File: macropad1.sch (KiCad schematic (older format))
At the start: 20 parts, among them J1 Conn_01x04, J2 USB_B_Mini, J3 AVR-ISP-6, SW1 SPST, SW2 Rotary_Encoder_Switch, U1 ATmega32U4-AU, U2 24LC512, Y1 16Mhz

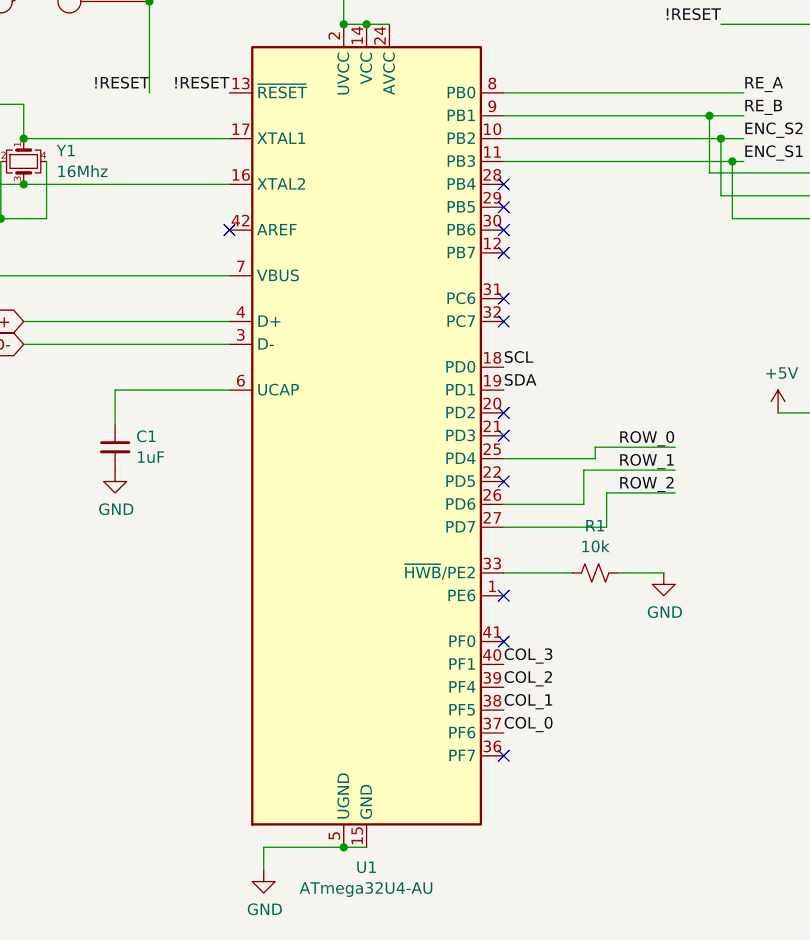
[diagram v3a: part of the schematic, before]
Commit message: Adds testpads for all unused pins on MCU
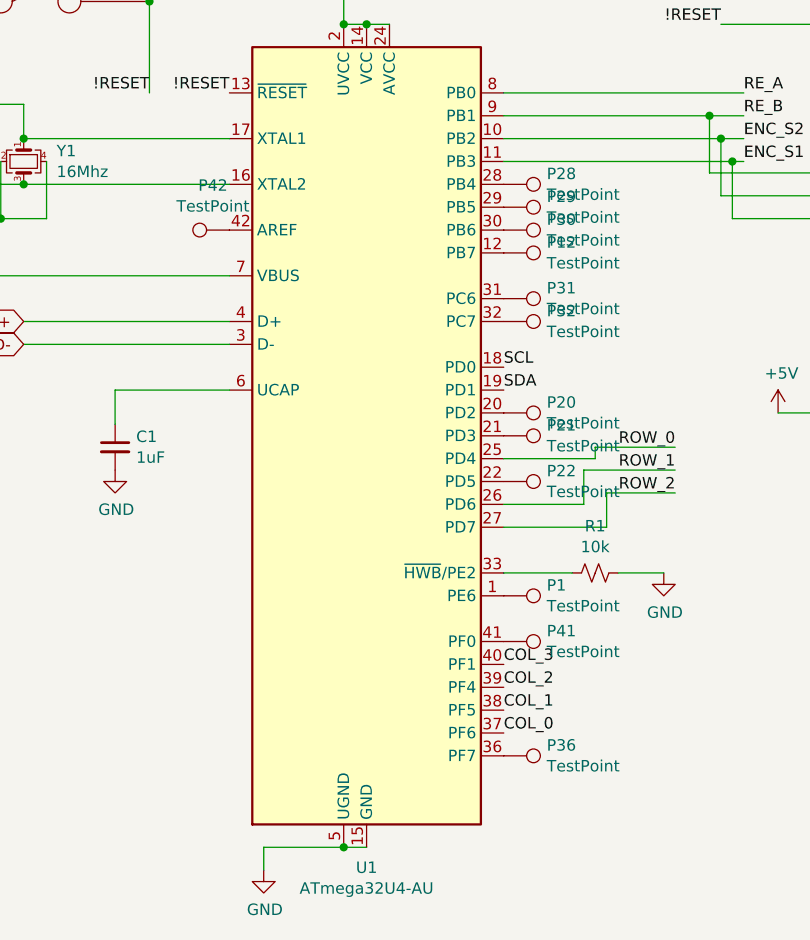
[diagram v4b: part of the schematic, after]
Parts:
- added P1, P12, P20, P21, P22, P28, P29, P30, P31, P32, P36, P41, P42: TestPoint, TestPoint:TestPoint_Pad_D1.0mm, symbol Connector:TestPoint
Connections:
- net at U1.1 (PE6): now also P1.1
- net at U1.12 (PB7): now also P12.1
- net at U1.20 (PD2): now also P20.1
- net at U1.21 (PD3): now also P21.1
- net at U1.22 (PD5): now also P22.1
- net at U1.28 (PB4): now also P28.1
- net at U1.29 (PB5): now also P29.1
- net at U1.30 (PB6): now also P30.1
- net at U1.31 (PC6): now also P31.1
- net at U1.32 (PC7): now also P32.1
- net at U1.36 (PF7): now also P36.1
- net at U1.41 (PF0): now also P41.1
- net at U1.42 (AREF): now also P42.1
- no-connect marks 14 -> 1
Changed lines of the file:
@@
 	1    0    0    -1
 $EndComp
-NoConn ~ 4500 2600
-NoConn ~ 4500 2700
-NoConn ~ 4500 2800
-NoConn ~ 4500 2900
-NoConn ~ 4500 3100
-NoConn ~ 4500 3200
-NoConn ~ 4500 3600
-NoConn ~ 4500 3700
-NoConn ~ 4500 3900
-NoConn ~ 4500 4400
-NoConn ~ 4500 4600
-NoConn ~ 4500 5100
 Wire Wire Line
 	6200 1450 6300 1450
@@
 Connection ~ 7250 4050
 NoConn ~ 7650 3850
-NoConn ~ 3300 2800
 Wire Wire Line
 	3300 3000 1150 3000
@@
 Wire Wire Line
 	6950 2150 6500 2150
+$Comp
+L Connector:TestPoint P28
+U 1 1 5F6F4AA3
+P 4500 2600
+F 0 "P28" V 4454 2788 50  0000 L CNN
+F 1 "TestPoint" V 4545 2788 50  0000 L CNN
+F 2 "TestPoint:TestPoint_Pad_D1.0mm" H 4700 2600 50  0001 C CNN
+F 3 "~" H 4700 2600 50  0001 C CNN
+	1    4500 2600
+	0    1    1    0
+$EndComp
+$Comp
+L Connector:TestPoint P29
+U 1 1 5F6F7A9F
+P 4500 2700
+F 0 "P29" V 4454 2888 50  0000 L CNN
+F 1 "TestPoint" V 4545 2888 50  0000 L CNN
+F 2 "TestPoint:TestPoint_Pad_D1.0mm" H 4700 2700 50  0001 C CNN
+F 3 "~" H 4700 2700 50  0001 C CNN
+	1    4500 2700
+	0    1    1    0
+$EndComp
+$Comp
+L Connector:TestPoint P30
+U 1 1 5F6F7EF0
+P 4500 2800
+F 0 "P30" V 4454 2988 50  0000 L CNN
+F 1 "TestPoint" V 4545 2988 50  0000 L CNN
+F 2 "TestPoint:TestPoint_Pad_D1.0mm" H 4700 2800 50  0001 C CNN
+F 3 "~" H 4700 2800 50  0001 C CNN
+	1    4500 2800
+	0    1    1    0
+$EndComp
+$Comp
+L Connector:TestPoint P12
+U 1 1 5F6F82A4
+P 4500 2900
+F 0 "P12" V 4454 3088 50  0000 L CNN
+F 1 "TestPoint" V 4545 3088 50  0000 L CNN
+F 2 "TestPoint:TestPoint_Pad_D1.0mm" H 4700 2900 50  0001 C CNN
+F 3 "~" H 4700 2900 50  0001 C CNN
+	1    4500 2900
+	0    1    1    0
+$EndComp
+$Comp
+L Connector:TestPoint P31
+U 1 1 5F6F8637
+P 4500 3100
+F 0 "P31" V 4454 3288 50  0000 L CNN
+F 1 "TestPoint" V 4545 3288 50  0000 L CNN
+F 2 "TestPoint:TestPoint_Pad_D1.0mm" H 4700 3100 50  0001 C CNN
+F 3 "~" H 4700 3100 50  0001 C CNN
+	1    4500 3100
+	0    1    1    0
+$EndComp
+$Comp
+L Connector:TestPoint P32
+U 1 1 5F6F8A2A
+P 4500 3200
+F 0 "P32" V 4454 3388 50  0000 L CNN
+F 1 "TestPoint" V 4545 3388 50  0000 L CNN
+F 2 "TestPoint:TestPoint_Pad_D1.0mm" H 4700 3200 50  0001 C CNN
+F 3 "~" H 4700 3200 50  0001 C CNN
+	1    4500 3200
+	0    1    1    0
+$EndComp
+$Comp
+L Connector:TestPoint P20
+U 1 1 5F6F8E3F
+P 4500 3600
+F 0 "P20" V 4454 3788 50  0000 L CNN
+F 1 "TestPoint" V 4545 3788 50  0000 L CNN
+F 2 "TestPoint:TestPoint_Pad_D1.0mm" H 4700 3600 50  0001 C CNN
+F 3 "~" H 4700 3600 50  0001 C CNN
+	1    4500 3600
+	0    1    1    0
+$EndComp
+$Comp
+L Connector:TestPoint P21
+U 1 1 5F6F92F7
+P 4500 3700
+F 0 "P21" V 4454 3888 50  0000 L CNN
+F 1 "TestPoint" V 4545 3888 50  0000 L CNN
+F 2 "TestPoint:TestPoint_Pad_D1.0mm" H 4700 3700 50  0001 C CNN
+F 3 "~" H 4700 3700 50  0001 C CNN
+	1    4500 3700
+	0    1    1    0
+$EndComp
+$Comp
+L Connector:TestPoint P22
+U 1 1 5F6F96DD
+P 4500 3900
+F 0 "P22" V 4454 4088 50  0000 L CNN
+F 1 "TestPoint" V 4545 4088 50  0000 L CNN
+F 2 "TestPoint:TestPoint_Pad_D1.0mm" H 4700 3900 50  0001 C CNN
+F 3 "~" H 4700 3900 50  0001 C CNN
+	1    4500 3900
+	0    1    1    0
+$EndComp
+$Comp
+L Connector:TestPoint P1
+U 1 1 5F6F9AE5
+P 4500 4400
+F 0 "P1" V 4454 4588 50  0000 L CNN
+F 1 "TestPoint" V 4545 4588 50  0000 L CNN
+F 2 "TestPoint:TestPoint_Pad_D1.0mm" H 4700 4400 50  0001 C CNN
+F 3 "~" H 4700 4400 50  0001 C CNN
+	1    4500 4400
+	0    1    1    0
+$EndComp
+$Comp
+L Connector:TestPoint P41
+U 1 1 5F6FA019
+P 4500 4600
+F 0 "P41" V 4454 4788 50  0000 L CNN
+F 1 "TestPoint" V 4545 4788 50  0000 L CNN
+F 2 "TestPoint:TestPoint_Pad_D1.0mm" H 4700 4600 50  0001 C CNN
+F 3 "~" H 4700 4600 50  0001 C CNN
+	1    4500 4600
+	0    1    1    0
+$EndComp
+$Comp
+L Connector:TestPoint P36
+U 1 1 5F6FC57F
+P 4500 5100
+F 0 "P36" V 4454 5288 50  0000 L CNN
+F 1 "TestPoint" V 4545 5288 50  0000 L CNN
+F 2 "TestPoint:TestPoint_Pad_D1.0mm" H 4700 5100 50  0001 C CNN
+F 3 "~" H 4700 5100 50  0001 C CNN
+	1    4500 5100
+	0    1    1    0
+$EndComp
+$Comp
+L Connector:TestPoint P42
+U 1 1 5F6FCA35
+P 3300 2800
+F 0 "P42" V 3495 2872 50  0000 C CNN
+F 1 "TestPoint" V 3404 2872 50  0000 C CNN
+F 2 "TestPoint:TestPoint_Pad_D1.0mm" H 3500 2800 50  0001 C CNN
+F 3 "~" H 3500 2800 50  0001 C CNN
+	1    3300 2800
+	0    -1   -1   0
+$EndComp
 $EndSCHEMATC

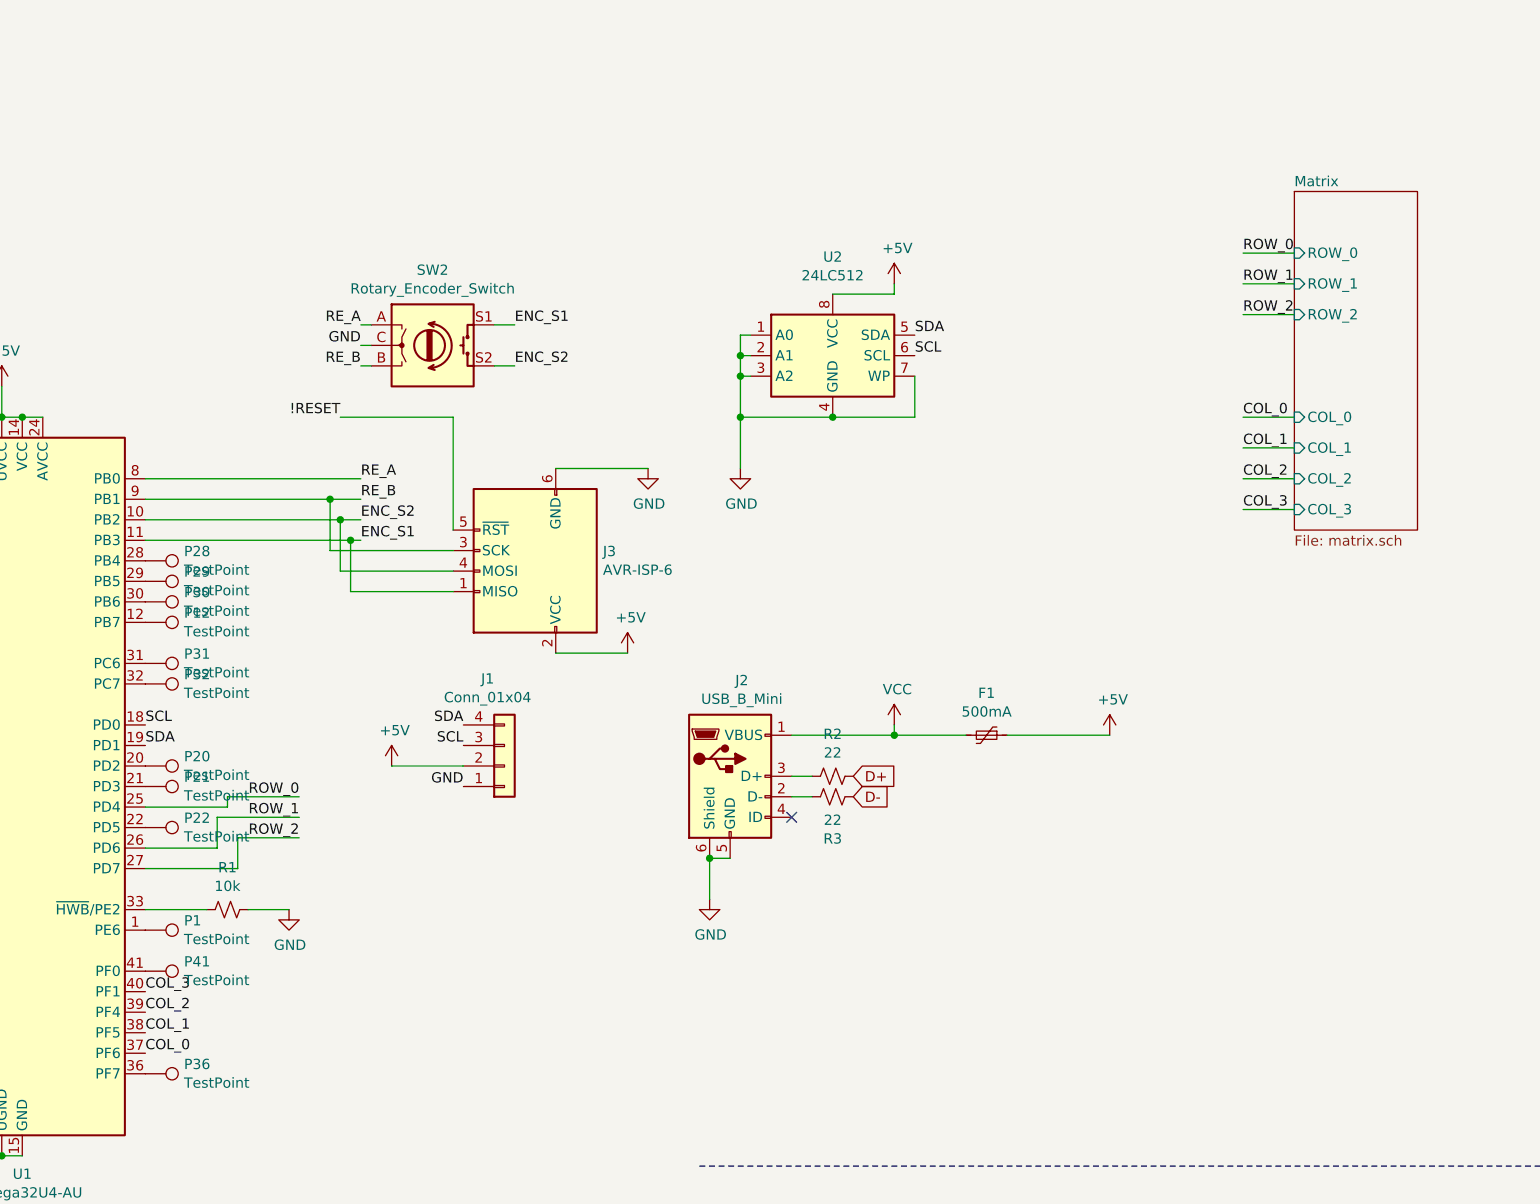
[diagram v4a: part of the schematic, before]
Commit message: Adds single color backlighting to each key :)
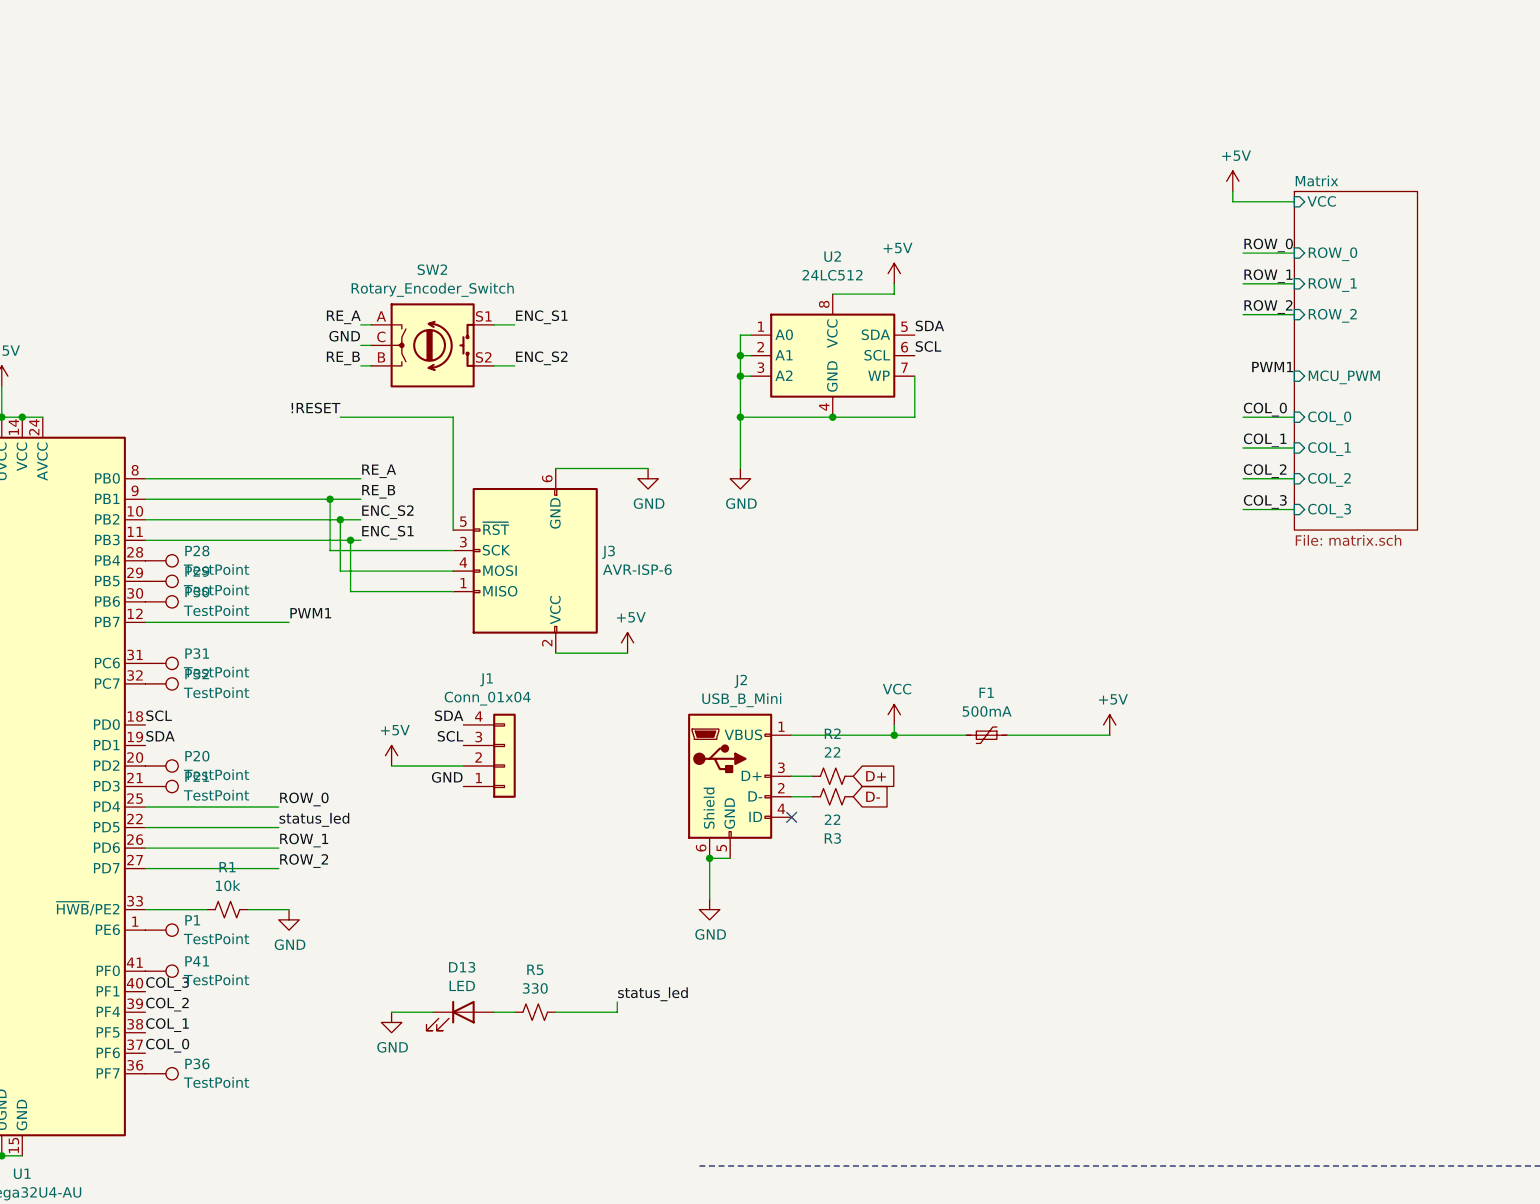
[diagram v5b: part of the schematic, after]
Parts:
- removed P12, P22: TestPoint, TestPoint:TestPoint_Pad_D1.0mm, symbol Connector:TestPoint
- added D13: LED, LED_SMD:LED_0805_2012Metric, symbol Device:LED
- added R5: 330, Resistor_SMD:R_0805_2012Metric, symbol Device:R_Small_US
- Y1: footprint Crystal:Crystal_SMD_3225-4Pin_3.2x2.5mm_HandSoldering -> Crystal:Crystal_SMD_3225-4Pin_3.2x2.5mm
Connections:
- net GND: now also D13.1 (K)
- net PWM1: now reaches U1.12 (PB7)
- net status_led: now reaches U1.22 (PD5)
- net status_led: now also R5.1
- new net: D13.2 (A), R5.2
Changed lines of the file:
@@
 F 0 "Y1" V 2354 2644 50  0000 L CNN
 F 1 "16Mhz" V 2445 2644 50  0000 L CNN
-F 2 "Crystal:Crystal_SMD_3225-4Pin_3.2x2.5mm_HandSoldering" H 2400 2500 50  0001 C CNN
+F 2 "Crystal:Crystal_SMD_3225-4Pin_3.2x2.5mm" H 2400 2500 50  0001 C CNN
 F 3 "~" H 2400 2500 50  0001 C CNN
 	1    2400 2500
@@
 F7 "COL_2" I L 10100 2200 50
 F8 "COL_3" I L 10100 2350 50
+F9 "MCU_PWM" I L 10100 1700 50
+F10 "VCC" I L 10100 850 50
 $EndSheet
 Wire Wire Line
@@
 Text Label 4500 5000 0    50   ~ 0
 COL_0
-Text Label 5250 3850 2    50   ~ 0
+Text Label 5150 4000 0    50   ~ 0
 ROW_1
-Text Label 5250 3750 2    50   ~ 0
+Text Label 5150 3800 0    50   ~ 0
 ROW_0
-Text Label 5250 3950 2    50   ~ 0
+Text Label 5150 4100 0    50   ~ 0
 ROW_2
 Text Label 4500 4800 0    50   ~ 0
@@
 Text Label 6050 3400 2    50   ~ 0
 SDA
-Wire Wire Line
-	5250 3750 4900 3750
-Wire Wire Line
-	4900 3750 4900 3800
-Wire Wire Line
-	4900 3800 4500 3800
-Wire Wire Line
-	5250 3850 4850 3850
-Wire Wire Line
-	4850 3850 4850 4000
-Wire Wire Line
-	4850 4000 4500 4000
-Wire Wire Line
-	5250 3950 4950 3950
-Wire Wire Line
-	4950 3950 4950 4100
-Wire Wire Line
-	4950 4100 4500 4100
 $Comp
 L Connector_Generic:Conn_01x04 J1
@@
 $EndComp
 $Comp
-L Connector:TestPoint P12
-U 1 1 5F6F82A4
-P 4500 2900
-F 0 "P12" V 4454 3088 50  0000 L CNN
-F 1 "TestPoint" V 4545 3088 50  0000 L CNN
-F 2 "TestPoint:TestPoint_Pad_D1.0mm" H 4700 2900 50  0001 C CNN
-F 3 "~" H 4700 2900 50  0001 C CNN
-	1    4500 2900
-	0    1    1    0
-$EndComp
-$Comp
 L Connector:TestPoint P31
 U 1 1 5F6F8637
@@
 F 3 "~" H 4700 3700 50  0001 C CNN
 	1    4500 3700
-	0    1    1    0
-$EndComp
-$Comp
-L Connector:TestPoint P22
-U 1 1 5F6F96DD
-P 4500 3900
-F 0 "P22" V 4454 4088 50  0000 L CNN
-F 1 "TestPoint" V 4545 4088 50  0000 L CNN
-F 2 "TestPoint:TestPoint_Pad_D1.0mm" H 4700 3900 50  0001 C CNN
-F 3 "~" H 4700 3900 50  0001 C CNN
-	1    4500 3900
 	0    1    1    0
 $EndComp
@@
 	0    -1   -1   0
 $EndComp
+Text Label 5150 3900 0    50   ~ 0
+status_led
+Wire Wire Line
+	4500 4100 5150 4100
+Wire Wire Line
+	4500 4000 5150 4000
+Wire Wire Line
+	4500 3800 5150 3800
+Wire Wire Line
+	5150 3900 4500 3900
+$Comp
+L Device:LED D13
+U 1 1 5F62114F
+P 6050 4800
+F 0 "D13" H 6043 5017 50  0000 C CNN
+F 1 "LED" H 6043 4926 50  0000 C CNN
+F 2 "LED_SMD:LED_0805_2012Metric" H 6050 4800 50  0001 C CNN
+F 3 "~" H 6050 4800 50  0001 C CNN
+	1    6050 4800
+	1    0    0    -1
+$EndComp
+$Comp
+L power:GND #PWR0120
+U 1 1 5F621EFB
+P 5700 4800
+F 0 "#PWR0120" H 5700 4550 50  0001 C CNN
+F 1 "GND" H 5705 4627 50  0000 C CNN
+F 2 "" H 5700 4800 50  0001 C CNN
+F 3 "" H 5700 4800 50  0001 C CNN
+	1    5700 4800
+	1    0    0    -1
+$EndComp
+Wire Wire Line
+	5700 4800 5900 4800
+$Comp
+L Device:R_Small_US R5
+U 1 1 5F62673C
+P 6400 4800
+F 0 "R5" V 6195 4800 50  0000 C CNN
+F 1 "330" V 6286 4800 50  0000 C CNN
+F 2 "Resistor_SMD:R_0805_2012Metric" H 6400 4800 50  0001 C CNN
+F 3 "~" H 6400 4800 50  0001 C CNN
+	1    6400 4800
+	0    1    1    0
+$EndComp
+Wire Wire Line
+	6200 4800 6300 4800
+Wire Wire Line
+	6500 4800 6800 4800
+Wire Wire Line
+	6800 4800 6800 4750
+Text Label 6800 4750 0    50   ~ 0
+status_led
+Wire Wire Line
+	9800 850  9800 800
+Wire Wire Line
+	9800 850  10100 850
+$Comp
+L power:+5V #PWR01
+U 1 1 5F6F79C5
+P 9800 800
+F 0 "#PWR01" H 9800 650 50  0001 C CNN
+F 1 "+5V" H 9815 973 50  0000 C CNN
+F 2 "" H 9800 800 50  0001 C CNN
+F 3 "" H 9800 800 50  0001 C CNN
+	1    9800 800
+	1    0    0    -1
+$EndComp
+Text Label 5200 2900 0    50   ~ 0
+PWM1
+Wire Wire Line
+	5200 2900 4500 2900
+Text Label 10100 1700 2    50   ~ 0
+PWM1
 $EndSCHEMATC
